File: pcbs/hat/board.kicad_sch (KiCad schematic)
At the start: 1 part, among them U1 NUCLEO-F401RE

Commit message: fix symbol and footprint libraries
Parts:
- U1: footprint ST_NUCLEO-F401RE -> STS_Boards:ST_Morpho_Connector_64_MountingHoles
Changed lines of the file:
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@@
       (effects (font (size 1.27 1.27)) (justify left))
     )
-    (property "Footprint" "ST_NUCLEO-F401RE" (id 2) (at 184.15 97.79 0)
+    (property "Footprint" "STS_Boards:ST_Morpho_Connector_64_MountingHoles" (id 2) (at 184.15 97.79 0)
       (effects (font (size 1.27 1.27)) (justify left bottom) hide)
     )
@@
     (property "Reference" "U1" (id 0) (at 246.38 30.48 0))
     (property "Value" "NUCLEO-F401RE" (id 1) (at 246.38 33.02 0))
-    (property "Footprint" "ST_NUCLEO-F401RE" (id 2) (at 241.3 45.72 0)
+    (property "Footprint" "STS_Boards:ST_Morpho_Connector_64_MountingHoles" (id 2) (at 241.3 45.72 0)
       (effects (font (size 1.27 1.27)) (justify left bottom) hide)
     )
@@
     (property "Reference" "U1" (id 0) (at 62.23 15.24 0))
     (property "Value" "NUCLEO-F401RE" (id 1) (at 62.23 17.78 0))
-    (property "Footprint" "ST_NUCLEO-F401RE" (id 2) (at 57.15 60.96 0)
+    (property "Footprint" "STS_Boards:ST_Morpho_Connector_64_MountingHoles" (id 2) (at 57.15 60.96 0)
       (effects (font (size 1.27 1.27)) (justify left bottom) hide)
     )
@@
       (effects (font (size 1.27 1.27)) (justify left))
     )
-    (property "Footprint" "ST_NUCLEO-F401RE" (id 2) (at 184.15 123.19 0)
+    (property "Footprint" "STS_Boards:ST_Morpho_Connector_64_MountingHoles" (id 2) (at 184.15 123.19 0)
       (effects (font (size 1.27 1.27)) (justify left bottom) hide)
     )
@@
     (property "Reference" "U1" (id 0) (at 132.08 20.32 0))
     (property "Value" "NUCLEO-F401RE" (id 1) (at 132.08 22.86 0))
-    (property "Footprint" "ST_NUCLEO-F401RE" (id 2) (at 127 63.5 0)
+    (property "Footprint" "STS_Boards:ST_Morpho_Connector_64_MountingHoles" (id 2) (at 127 63.5 0)
       (effects (font (size 1.27 1.27)) (justify left bottom) hide)
     )
@@
     (property "Reference" "U1" (id 0) (at 194.31 41.91 0))
     (property "Value" "NUCLEO-F401RE" (id 1) (at 194.31 44.45 0))
-    (property "Footprint" "ST_NUCLEO-F401RE" (id 2) (at 189.23 62.23 0)
-      (effects (font (size 1.27 1.27)) (justify left bottom) hide)
-    )
+    (property "Footprint" "STS_Boards:ST_Morpho_Connector_64_MountingHoles" (id 2) (at 189.23 62.23 0)
+      (effects (font (size 1.27 1.27)) (justify left bottom) hide)
+    )

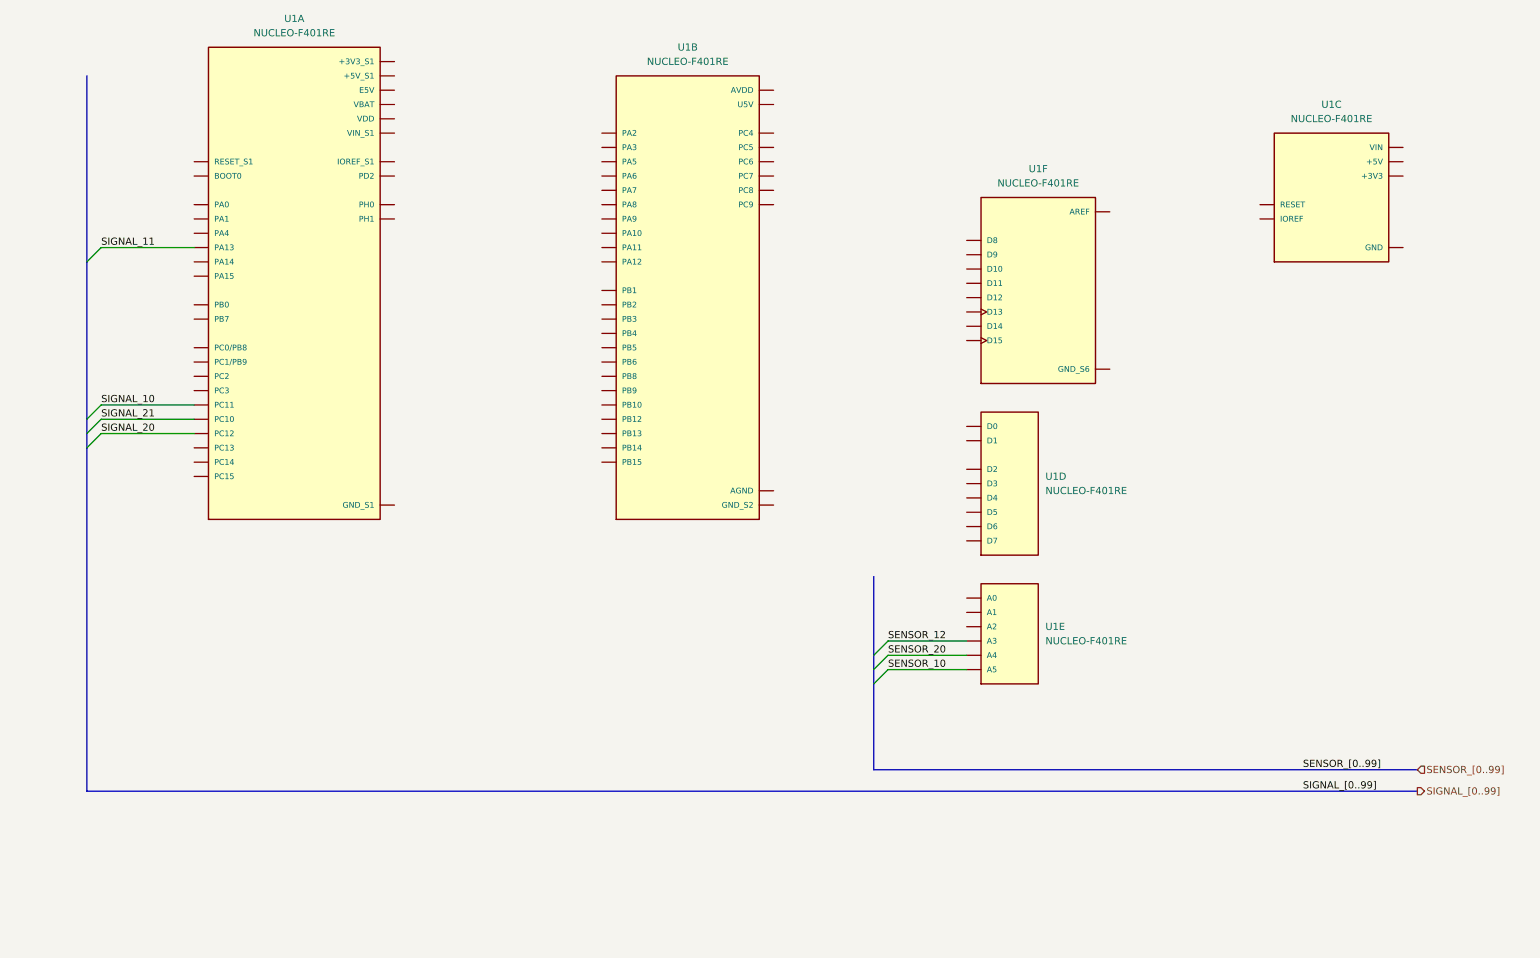
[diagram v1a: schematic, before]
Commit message: add ADCs
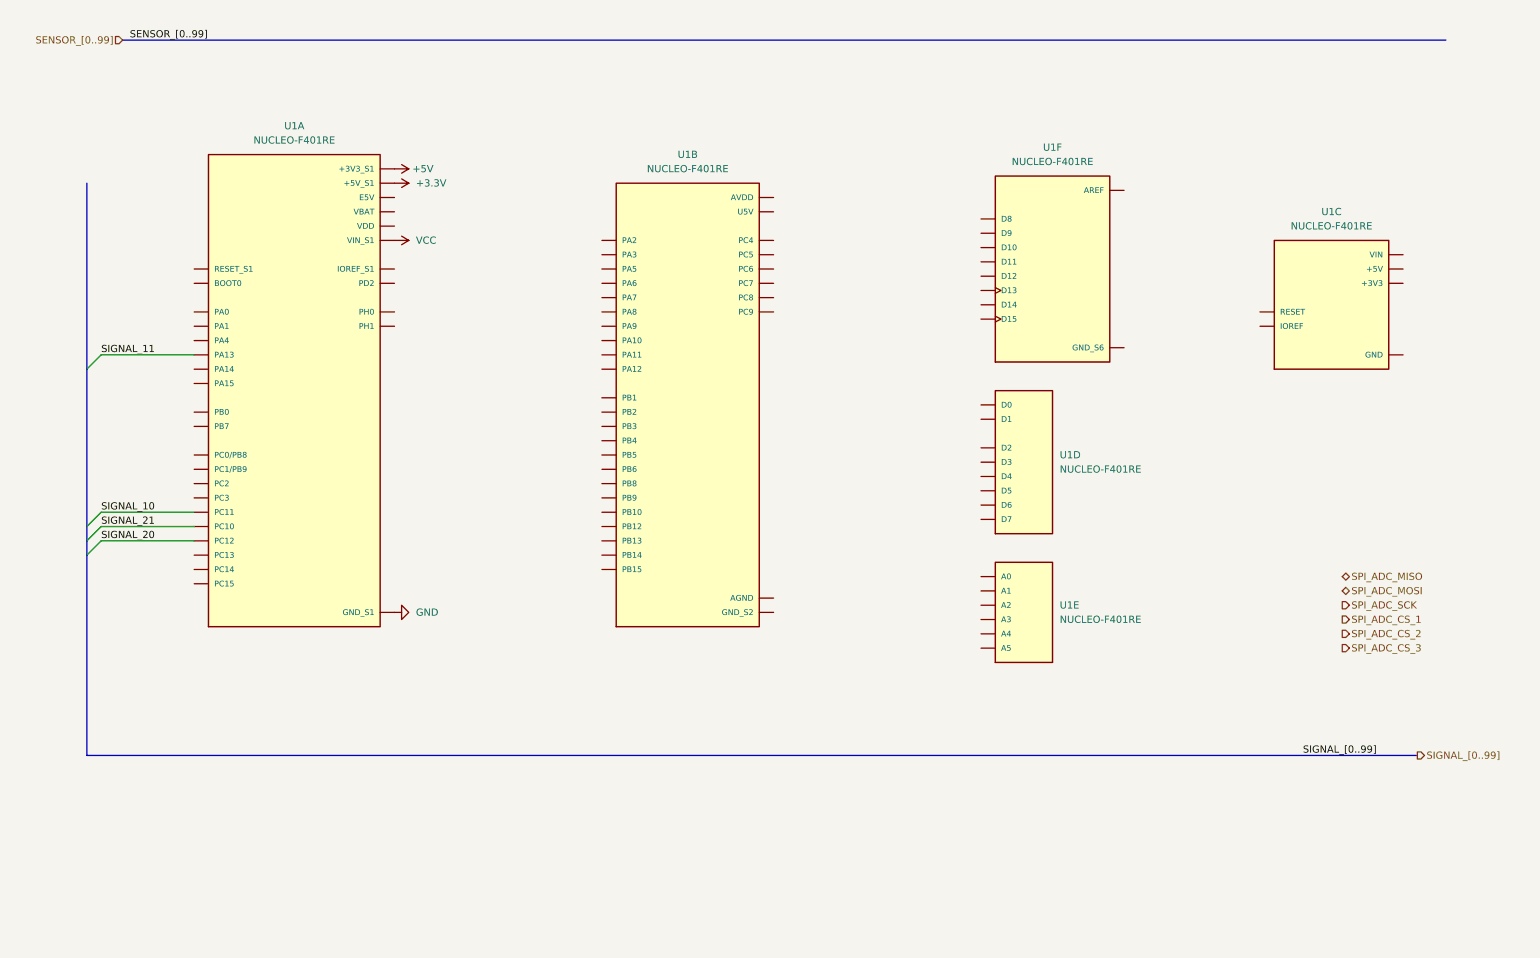
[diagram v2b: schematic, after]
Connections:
- net +5V: now reaches U1.CN7_16 (+3V3_S1)
- net +3.3V: now reaches U1.CN7_18 (+5V_S1)
- net GND: now reaches U1.CN7_19 (GND_S1), U1.CN7_20 (GND_S1), U1.CN7_22 (GND_S1), U1.CN7_8 (GND_S1)
- net VCC: now reaches U1.CN7_24 (VIN_S1)
- net SENSOR_10: no longer names the net of U1.CN8_6 (A5)
- net SENSOR_12: no longer names the net of U1.CN8_4 (A3)
- net SENSOR_20: no longer names the net of U1.CN8_5 (A4)
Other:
- moved on the sheet: U1A, U1B, U1C, U1D, U1E, U1F

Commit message: work on charging circuit
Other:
- note added: "Datasheet CPU"
- note added: "Datasheet Nucleo Board"
- note added: "GPIO Out: 3.3V 8ma GPIO In: 5V 8ma ADC: 3.3V Max"
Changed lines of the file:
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@@
     (stroke (width 0) (type default) (color 0 0 0 0))
+  )
+  (text "Datasheet Nucleo Board" (at 35.56 161.29 0)
+    (effects (font (size 1.27 1.27)) (justify left bottom))
+  )
+  (text "GPIO Out: 3.3V 8ma\nGPIO In: 5V 8ma\nADC: 3.3V Max\n\n"
+    (at 29.21 177.8 0)
+    (effects (font (size 1.27 1.27)) (justify left bottom))
+  )
+  (text "Datasheet CPU" (at 35.56 165.1 0)
+    (effects (font (size 1.27 1.27)) (justify left bottom))
   )
   (label "SIGNAL_[0..99]" (at 241.3 146.05 0)
@@
     (pin "1")
   )
+  (symbol (lib_id "STS_Other:Link") (at 31.75 161.29 0) (unit 1)
+    (in_bom yes) (on_board yes) (fields_autoplaced)
+    (property "Reference" "#Z17" (id 0) (at 31.75 157.734 0)
+      (effects (font (size 1.27 1.27)) hide)
+    )
+    (property "Value" "Link" (id 1) (at 33.02 157.734 0)
+      (effects (font (size 1.27 1.27)) (justify right) hide)
+    )
+    (property "Footprint" "" (id 2) (at 29.21 159.004 0)
+      (effects (font (size 1.27 1.27)) hide)
+    )
+    (property "Datasheet" "https://www.st.com/resource/en/user_manual/dm00387966-stm32-nucleo-64-p-boards-stmicroelectronics.pdf" (id 3) (at 29.21 159.004 0)
+      (effects (font (size 1.27 1.27)) hide)
+    )
+  )
   (symbol (lib_id "STS_Boards:NUCLEO-F401RE") (at 191.77 119.38 0) (unit 5)
     (in_bom yes) (on_board yes) (fields_autoplaced)
@@
     (pin "1")
   )
+  (symbol (lib_id "STS_Other:Link") (at 31.75 165.1 0) (unit 1)
+    (in_bom yes) (on_board yes) (fields_autoplaced)
+    (property "Reference" "#Z18" (id 0) (at 31.75 161.544 0)
+      (effects (font (size 1.27 1.27)) hide)
+    )
+    (property "Value" "Link" (id 1) (at 33.02 161.544 0)
+      (effects (font (size 1.27 1.27)) (justify right) hide)
+    )
+    (property "Footprint" "" (id 2) (at 29.21 162.814 0)
+      (effects (font (size 1.27 1.27)) hide)
+    )
+    (property "Datasheet" "https://www.st.com/en/microcontrollers-microprocessors/stm32f411re.html?rt=db&id=DB2196" (id 3) (at 29.21 162.814 0)
+      (effects (font (size 1.27 1.27)) hide)
+    )
+  )
   (symbol (lib_id "STS_Boards:NUCLEO-F401RE") (at 132.08 82.55 0) (unit 2)

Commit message: more work on charging circuit
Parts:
- renumbered U1 to U17
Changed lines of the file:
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@@
   (symbol (lib_id "STS_Boards:NUCLEO-F401RE") (at 191.77 93.98 0) (unit 4)
     (in_bom yes) (on_board yes) (fields_autoplaced)
-    (property "Reference" "U1" (id 0) (at 198.12 92.7099 0)
+    (property "Reference" "U17" (id 0) (at 198.12 92.7099 0)
       (effects (font (size 1.27 1.27)) (justify left))
     )
@@
   (symbol (lib_id "STS_Boards:NUCLEO-F401RE") (at 246.38 64.77 0) (unit 3)
     (in_bom yes) (on_board yes) (fields_autoplaced)
-    (property "Reference" "U1" (id 0) (at 246.38 49.53 0))
+    (property "Reference" "U17" (id 0) (at 246.38 49.53 0))
     (property "Value" "NUCLEO-F401RE" (id 1) (at 246.38 52.07 0))
     (property "Footprint" "STS_Boards:ST_Morpho_Connector_64_MountingHoles" (id 2) (at 241.3 64.77 0)
@@
   (symbol (lib_id "STS_Boards:NUCLEO-F401RE") (at 62.23 80.01 0) (unit 1)
     (in_bom yes) (on_board yes) (fields_autoplaced)
-    (property "Reference" "U1" (id 0) (at 62.23 34.29 0))
+    (property "Reference" "U17" (id 0) (at 62.23 34.29 0))
     (property "Value" "NUCLEO-F401RE" (id 1) (at 62.23 36.83 0))
     (property "Footprint" "STS_Boards:ST_Morpho_Connector_64_MountingHoles" (id 2) (at 57.15 80.01 0)
@@
   (symbol (lib_id "power:+3.3V") (at 80.01 44.45 270) (unit 1)
     (in_bom yes) (on_board yes) (fields_autoplaced)
-    (property "Reference" "#PWR0200" (id 0) (at 76.2 44.45 0)
+    (property "Reference" "#PWR0132" (id 0) (at 76.2 44.45 0)
       (effects (font (size 1.27 1.27)) hide)
     )
@@
   (symbol (lib_id "STS_Boards:NUCLEO-F401RE") (at 191.77 119.38 0) (unit 5)
     (in_bom yes) (on_board yes) (fields_autoplaced)
-    (property "Reference" "U1" (id 0) (at 198.12 119.3799 0)
+    (property "Reference" "U17" (id 0) (at 198.12 119.3799 0)
       (effects (font (size 1.27 1.27)) (justify left))
     )
@@
   (symbol (lib_id "power:+5V") (at 80.01 41.91 270) (unit 1)
     (in_bom yes) (on_board yes) (fields_autoplaced)
-    (property "Reference" "#PWR0199" (id 0) (at 76.2 41.91 0)
+    (property "Reference" "#PWR0131" (id 0) (at 76.2 41.91 0)
       (effects (font (size 1.27 1.27)) hide)
     )
@@
   (symbol (lib_id "power:VCC") (at 80.01 54.61 270) (unit 1)
     (in_bom yes) (on_board yes) (fields_autoplaced)
-    (property "Reference" "#PWR0202" (id 0) (at 76.2 54.61 0)
+    (property "Reference" "#PWR0133" (id 0) (at 76.2 54.61 0)
       (effects (font (size 1.27 1.27)) hide)
     )
@@
   (symbol (lib_id "STS_Boards:NUCLEO-F401RE") (at 132.08 82.55 0) (unit 2)
     (in_bom yes) (on_board yes) (fields_autoplaced)
-    (property "Reference" "U1" (id 0) (at 132.08 39.37 0))
+    (property "Reference" "U17" (id 0) (at 132.08 39.37 0))
     (property "Value" "NUCLEO-F401RE" (id 1) (at 132.08 41.91 0))
     (property "Footprint" "STS_Boards:ST_Morpho_Connector_64_MountingHoles" (id 2) (at 127 82.55 0)
@@
   (symbol (lib_id "STS_Boards:NUCLEO-F401RE") (at 196.85 58.42 0) (unit 6)
     (in_bom yes) (on_board yes) (fields_autoplaced)
-    (property "Reference" "U1" (id 0) (at 196.85 38.1 0))
+    (property "Reference" "U17" (id 0) (at 196.85 38.1 0))
     (property "Value" "NUCLEO-F401RE" (id 1) (at 196.85 40.64 0))
     (property "Footprint" "STS_Boards:ST_Morpho_Connector_64_MountingHoles" (id 2) (at 191.77 58.42 0)
@@
   (symbol (lib_id "power:GND") (at 80.01 120.65 90) (unit 1)
     (in_bom yes) (on_board yes) (fields_autoplaced)
-    (property "Reference" "#PWR0201" (id 0) (at 86.36 120.65 0)
-      (effects (font (size 1.27 1.27)) hide)
-    )
+    (property "Reference" "#PWR0134" (id 0) (at 86.36 120.65 0)
+      (effects (font (size 1.27 1.27)) hide)
+    )

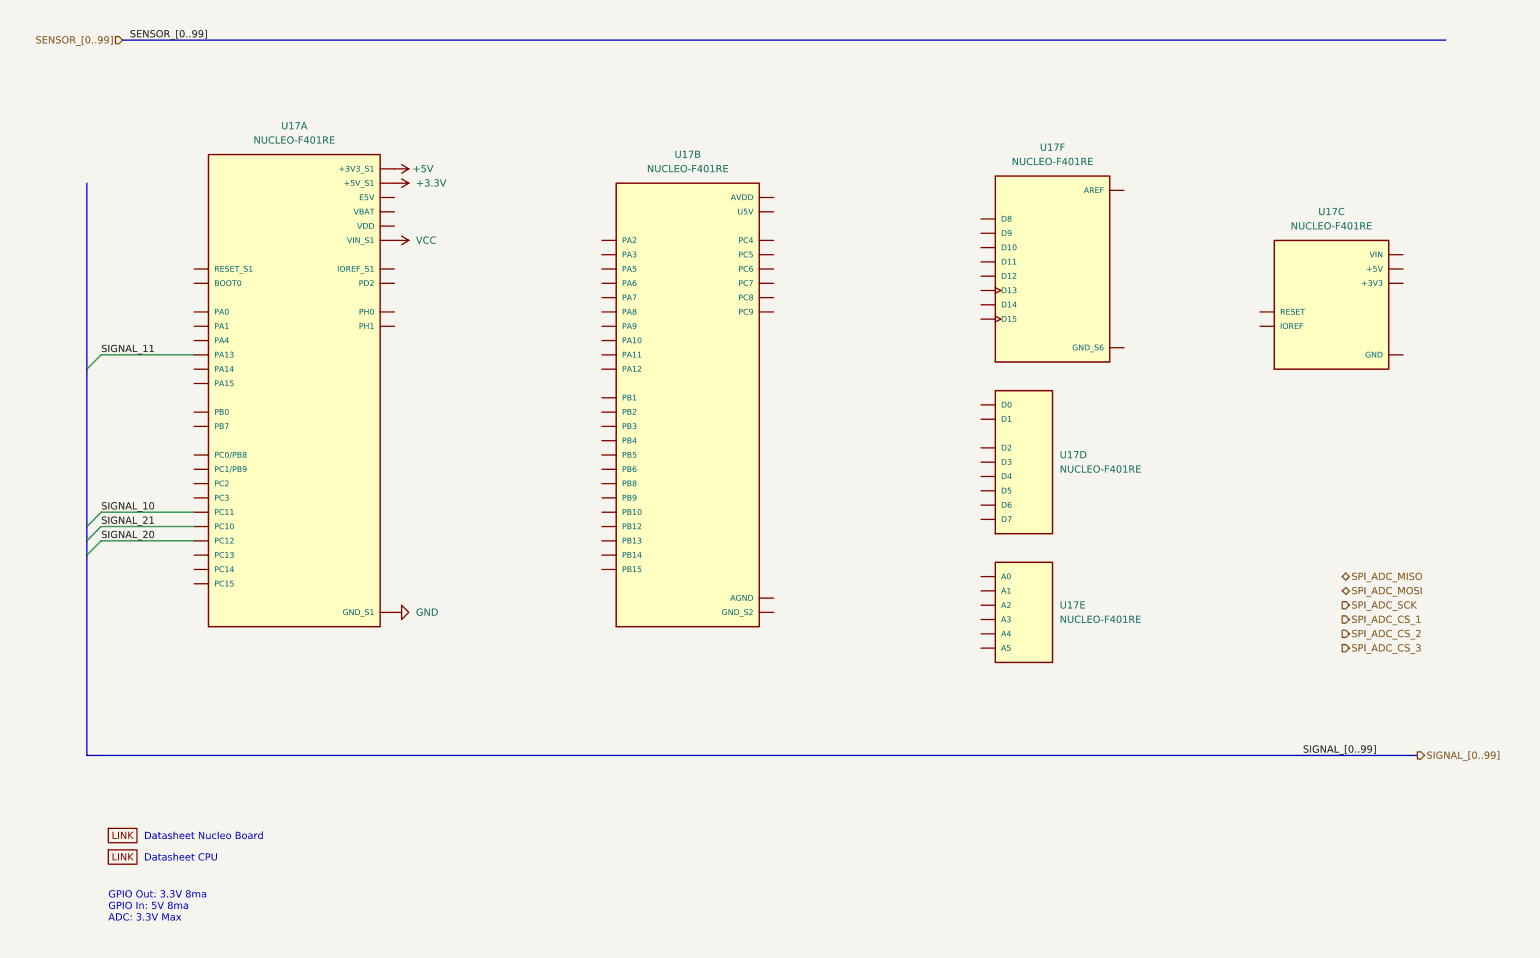
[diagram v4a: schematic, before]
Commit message: change ADCs and connect all Sensors and Signals
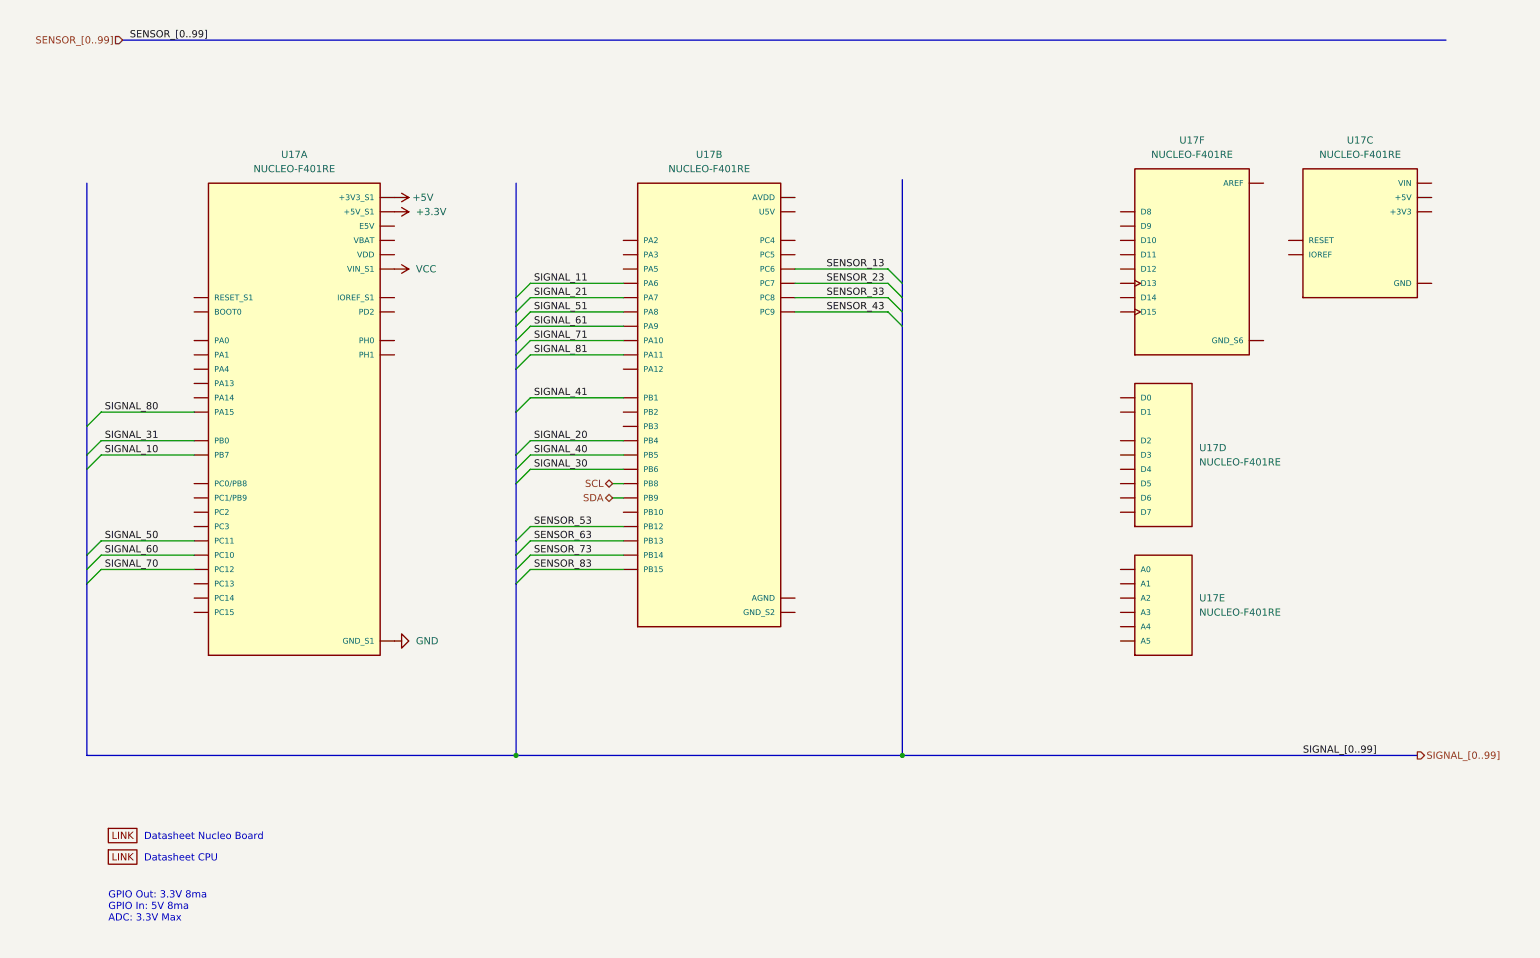
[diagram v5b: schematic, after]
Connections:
- net SIGNAL_10: now also U17.CN7_21 (PB7); no longer U17.CN7_2 (PC11)
- net SIGNAL_11: now also U17.CN10_13 (PA6); no longer U17.CN7_13 (PA13)
- net SIGNAL_20: now also U17.CN10_27 (PB4); no longer U17.CN7_3 (PC12)
- net SIGNAL_21: now also U17.CN10_15 (PA7); no longer U17.CN7_1 (PC10)
- net SIGNAL_80: now reaches U17.CN7_17 (PA15)
- net SIGNAL_31: now reaches U17.CN7_34 (PB0)
- net SENSOR_43: now reaches U17.CN10_1 (PC9)
- net SIGNAL_81: now reaches U17.CN10_14 (PA11)
- net SENSOR_53: now reaches U17.CN10_16 (PB12)
- net SIGNAL_30: now reaches U17.CN10_17 (PB6)
- net SENSOR_23: now reaches U17.CN10_19 (PC7)
- net SENSOR_33: now reaches U17.CN10_2 (PC8)
- net SIGNAL_61: now reaches U17.CN10_21 (PA9)
- net SIGNAL_51: now reaches U17.CN10_23 (PA8)
- net SIGNAL_41: now reaches U17.CN10_24 (PB1)
- net SENSOR_83: now reaches U17.CN10_26 (PB15)
- net SENSOR_73: now reaches U17.CN10_28 (PB14)
- net SIGNAL_40: now reaches U17.CN10_29 (PB5)
- net SCL: now reaches U17.CN10_3 (PB8)
- net SENSOR_63: now reaches U17.CN10_30 (PB13)
- net SIGNAL_71: now reaches U17.CN10_33 (PA10)
- net SENSOR_13: now reaches U17.CN10_4 (PC6)
- net SDA: now reaches U17.CN10_5 (PB9)
- new net SIGNAL_50: U17.CN7_2 (PC11)
- new net SIGNAL_60: U17.CN7_1 (PC10)
- new net SIGNAL_70: U17.CN7_3 (PC12)
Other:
- moved on the sheet: U17A, U17B, U17C, U17D, U17E, U17F
